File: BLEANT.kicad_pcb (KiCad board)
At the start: 4 copper layers, 75.8 x 76.2 mm, 71 parts, among them IC1 FAN4010IL6X_F113, IC2 FAN4010IL6X_F113, J1 Conn_01x04_Male, J2 SC_19-20, J3 Conn_01x02, J4 Conn_01x02, J5 1909763-1, U1 nRF51x22-QFxx, U2 LM50BIM3, U3 MP5077GG-Z, U4 MP5077GG-Z, U5 MCP2515-xSO, U6 SN65HVD1050D, X2 32.768kHz, Y1 16MHz

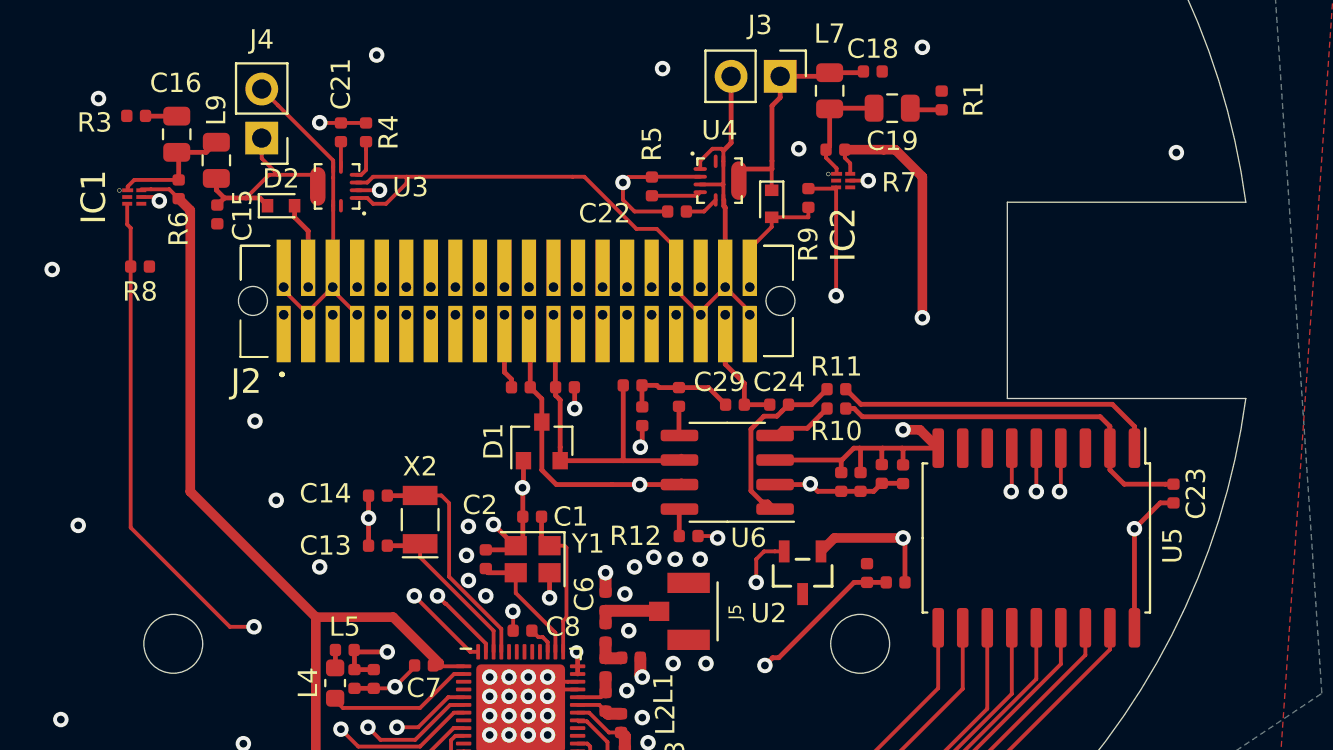
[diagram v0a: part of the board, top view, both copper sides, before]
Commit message: Added a level shifter
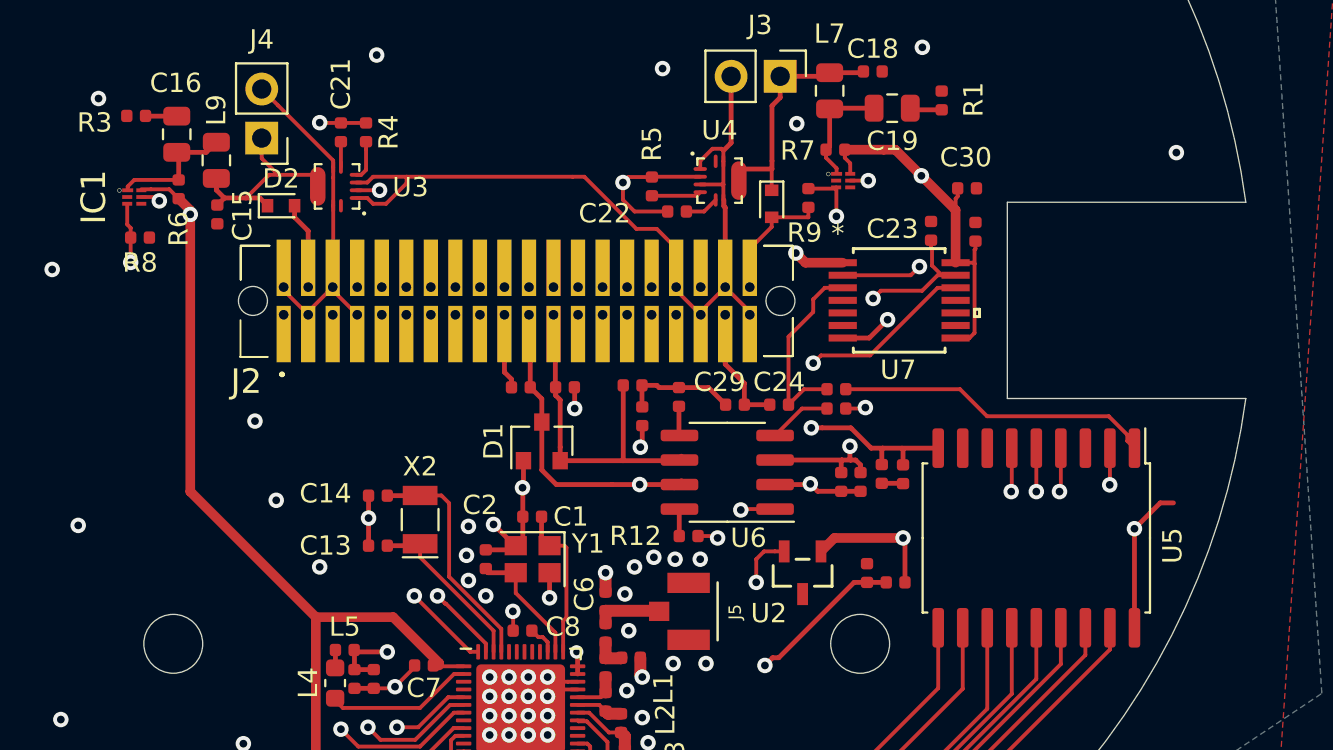
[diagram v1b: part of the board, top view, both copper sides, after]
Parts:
- added C30: 1nF, Capacitor_SMD:C_0402_1005Metric, F.Cu at (175.7, 121.2)
- added R16: 10k, Resistor_SMD:R_0402_1005Metric, F.Cu at (176.2, 123.5)
- added U7: TXB0104PWR, Level Shifter:TXB0104PWR, F.Cu at (172.2, 127.0)
- moved C23 18.5 mm to (173.8, 123.4), turned to 90 degrees
- moved R8 1.50 mm to (132.9, 123.8)
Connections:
- C17 pad 1: +5V -> +3V3
- C20 pad 2: +5V -> +3V3
- U5 pad 2: Net-(C23-Pad1) -> Net-(U5-Pad2)
- U5 pad 9: +5V -> +3V3
- U6 pad 1: Net-(C24-Pad2) -> Net-(U6-Pad1)
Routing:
- net +3V3: track 67.7 -> 122.6 mm, vias 0 -> 3
- net Net-(U5-Pad2): track 0.00 -> 22.2 mm, vias 0 -> 2
- net Net-(U6-Pad1): track 0.00 -> 21.0 mm, vias 0 -> 2
- net +5V: track 46.8 -> 54.9 mm
- net Net-(C23-Pad1): track 19.9 -> 14.4 mm, vias 0 -> 2
- net GND: track 84.1 -> 85.6 mm, vias 74 -> 75
- net 3V3Sense: track 40.7 -> 40.0 mm

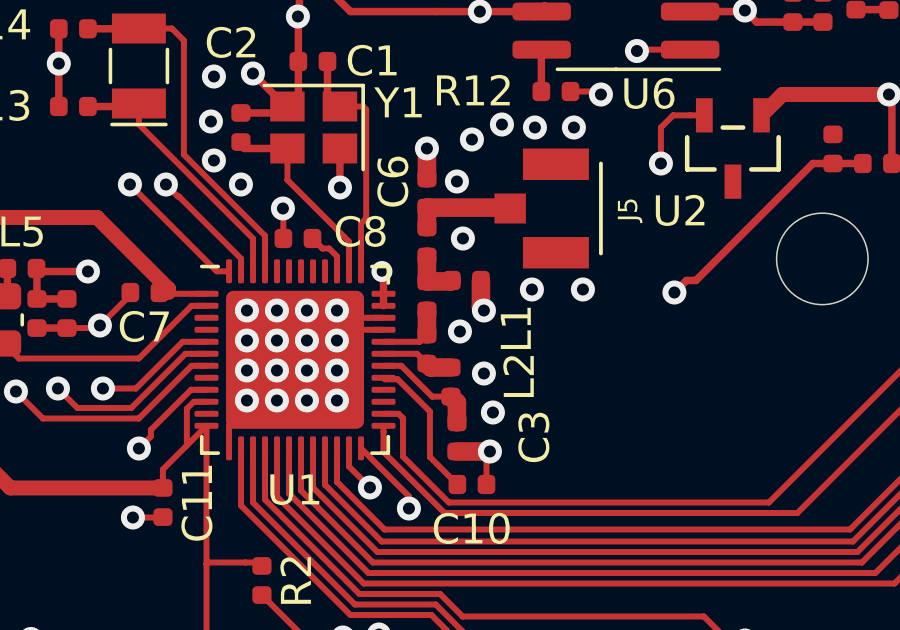
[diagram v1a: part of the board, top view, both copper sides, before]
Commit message: Changed RF traces to 50Ohm microstrips
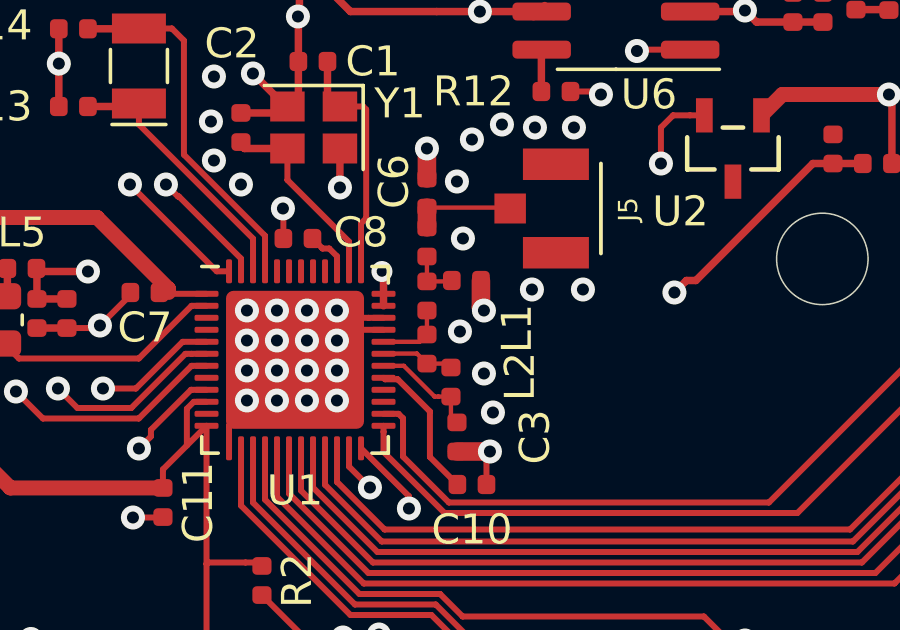
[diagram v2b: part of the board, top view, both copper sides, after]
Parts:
- U7: value TXB0104PWR -> PW14
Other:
- rule trace_min: 0.2 -> 0.1

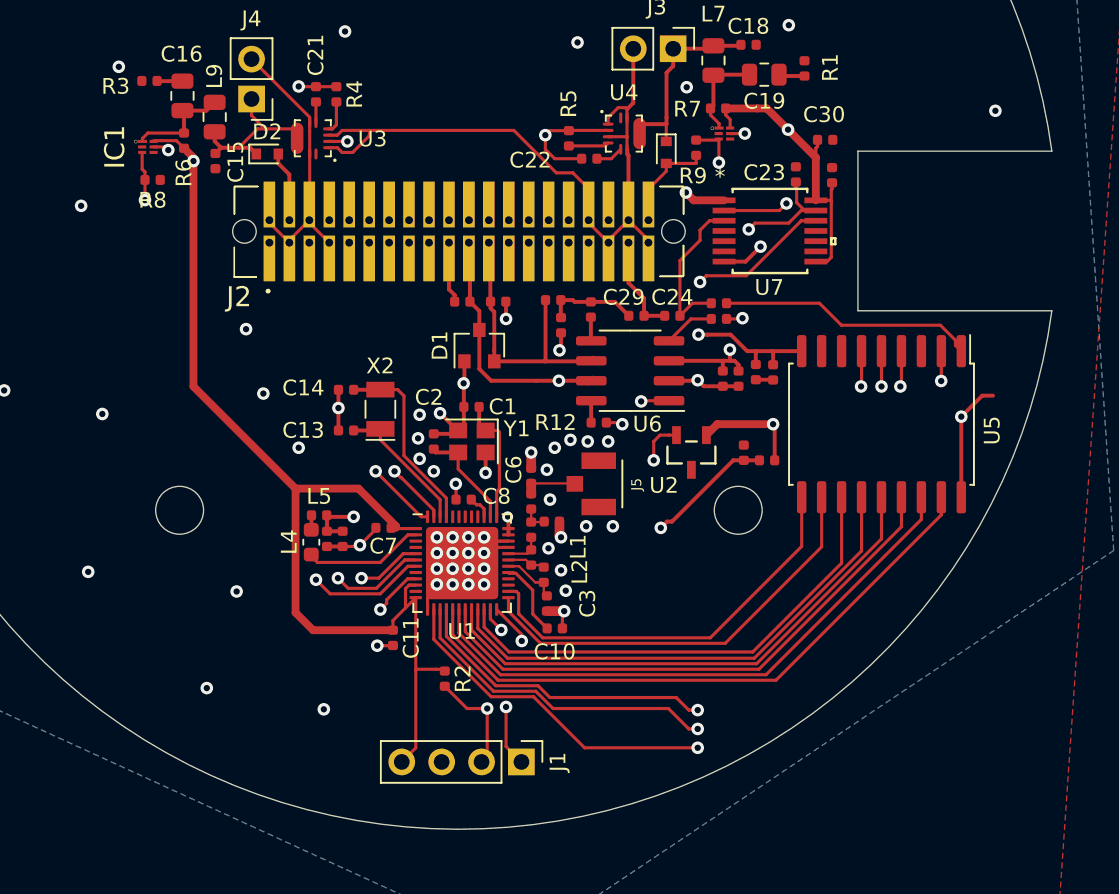
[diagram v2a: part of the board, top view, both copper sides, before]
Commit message: Added the filter and other alterations to routing. Removed copper peninsulas and improved routing overall
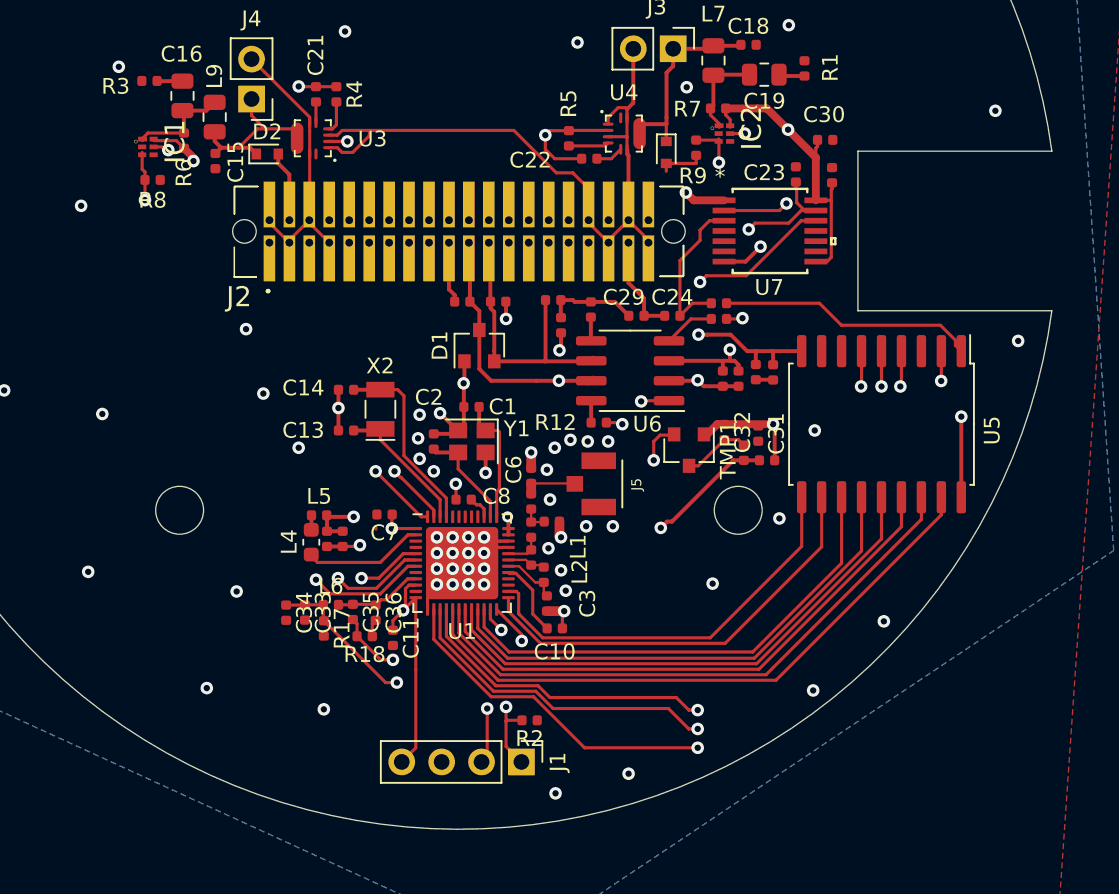
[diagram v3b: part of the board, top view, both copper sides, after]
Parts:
- removed U2: LM50BIM3, footprints:LM50_DBZ_3
- added C31: 1nF, Capacitor_SMD:C_0402_1005Metric, F.Cu at (171.4, 139.9)
- added C32: 100nF, Capacitor_SMD:C_0402_1005Metric, F.Cu at (169.3, 139.8)
- added C33: 1nF, Capacitor_SMD:C_0402_1005Metric, F.Cu at (142.6, 151.3)
- added C34: 100nF, Capacitor_SMD:C_0402_1005Metric, F.Cu at (141.4, 151.3)
- added C35: 100nF, Capacitor_SMD:C_0402_1005Metric, F.Cu at (145.7, 151.2)
- added C36: 2.2uF, Capacitor_SMD:C_0402_1005Metric, F.Cu at (147.1, 151.3)
- added L6: 2.2uH, Inductor_SMD:L_0402_1005Metric, F.Cu at (144.2, 150.8)
- added R17: 3.3k, Resistor_SMD:R_0402_1005Metric, F.Cu at (143.8, 152.3)
- added R18: 3.3, Resistor_SMD:R_0402_1005Metric, F.Cu at (146.4, 152.8)
- added TMP1: LM50CIM3X, Package_TO_SOT_SMD:SOT-23, F.Cu at (167.1, 140.9)
- IC1, IC2: footprint FAN4010:6-LEAD_MICROPAK -> MASA_Library:6-LEAD_MICROPAK
- R2: value 10k -> 1k
- U7: value PW14 -> TXB0104PWR
- moved R2 6.02 mm to (156.9, 158.2), turned to 180 degrees
- moved C7 0.85 mm to (147.7, 145.1)
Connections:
- R2 pad 1: +3V3 -> GND
- R2 pad 2: SWDIO -> SWDCLK
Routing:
- net +3V3: track 122.6 -> 32.4 mm, vias 3 -> 5
- net Net-(C33-Pad1): track 0.00 -> 47.0 mm, vias 0 -> 2
- net Temperature: track 45.6 -> 5.65 mm, vias 2 -> 0
- net SWDIO: track 14.6 -> 11.3 mm
- net GND: track 85.6 -> 87.4 mm, vias 75 -> 83
- net Net-(C36-Pad2): track 0.00 -> 1.10 mm
- net SWDCLK: track 11.2 -> 12.2 mm
- added copper zone on B.Cu, net +3V3
- removed copper zone on B.Cu, net GND

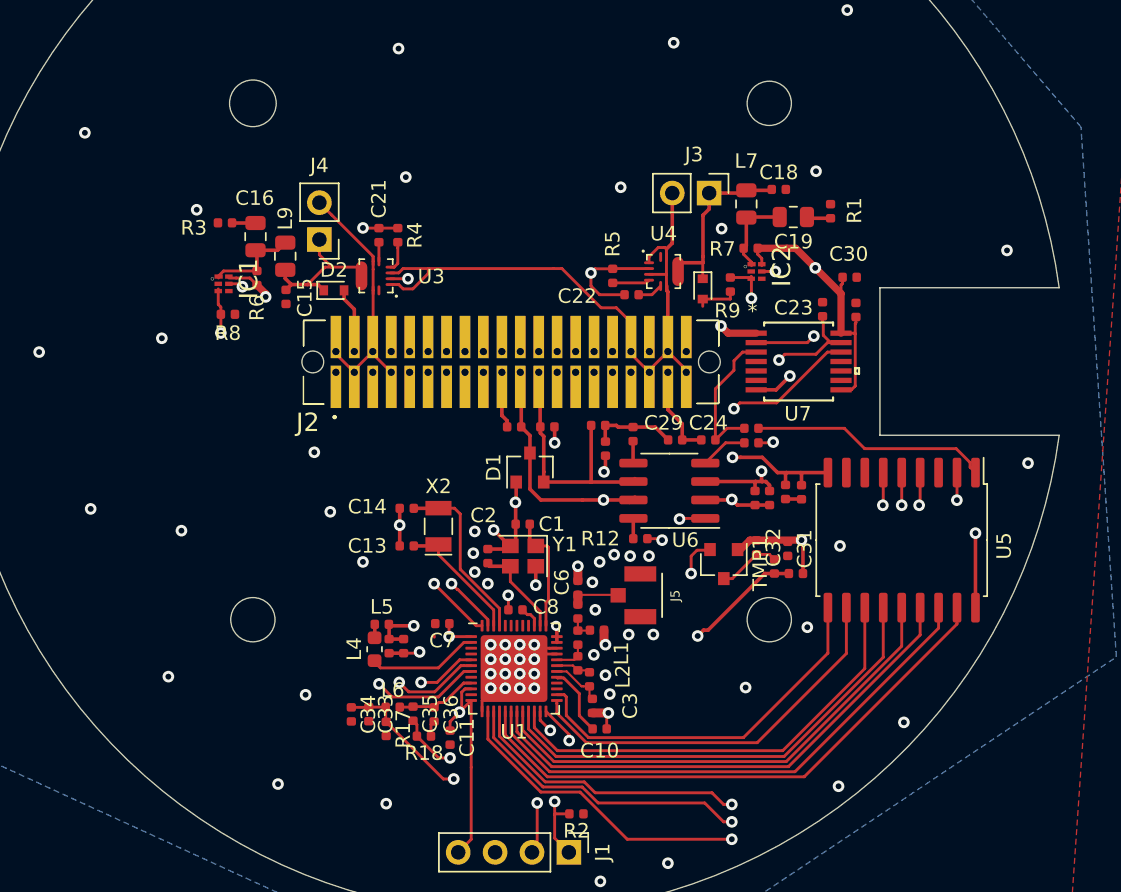
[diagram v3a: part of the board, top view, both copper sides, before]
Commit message: Added a metric ton of test points
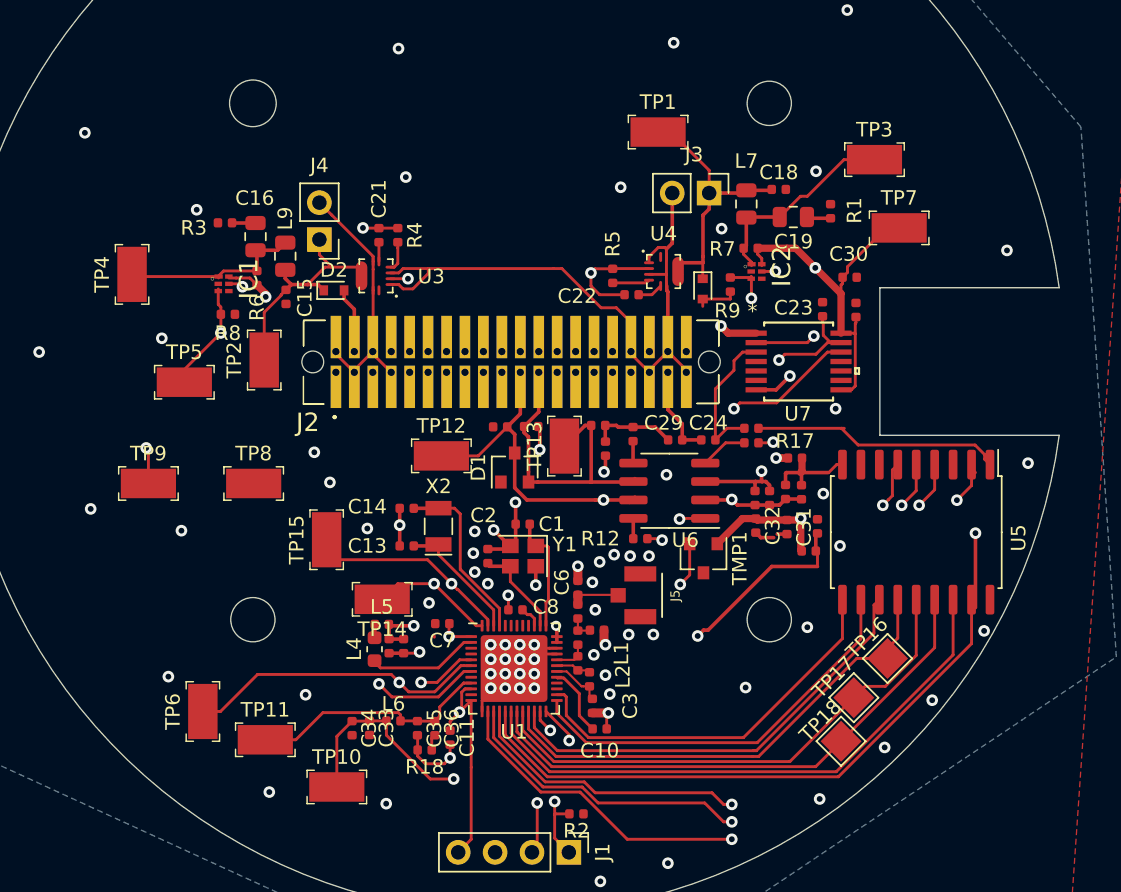
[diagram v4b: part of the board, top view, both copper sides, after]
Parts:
- added TP1: 5029, digikey-footprints:PC_Test_Point_Mini_3.8x2.03mm, F.Cu at (162.5, 111.2)
- added TP10: 5029, digikey-footprints:PC_Test_Point_Mini_3.8x2.03mm, F.Cu at (140.4, 156.3)
- added TP11: 5029, digikey-footprints:PC_Test_Point_Mini_3.8x2.03mm, F.Cu at (135.5, 153.1)
- added TP12: 5029, digikey-footprints:PC_Test_Point_Mini_3.8x2.03mm, F.Cu at (147.6, 133.5)
- added TP13: 5029, digikey-footprints:PC_Test_Point_Mini_3.8x2.03mm, F.Cu at (156.1, 132.8)
- added TP14: 5029, digikey-footprints:PC_Test_Point_Mini_3.8x2.03mm, F.Cu at (143.5, 143.4)
- added TP15: 5029, digikey-footprints:PC_Test_Point_Mini_3.8x2.03mm, F.Cu at (139.7, 139.3)
- added TP16: TestPoint, TestPoint:TestPoint_Pad_2.0x2.0mm, F.Cu at (178.3, 147.4)
- added TP17: TestPoint, TestPoint:TestPoint_Pad_2.0x2.0mm, F.Cu at (176.0, 150.2)
- added TP18: TestPoint, TestPoint:TestPoint_Pad_2.0x2.0mm, F.Cu at (175.1, 153.2)
- added TP2: 5029, digikey-footprints:PC_Test_Point_Mini_3.8x2.03mm, F.Cu at (135.4, 126.9)
- added TP3: 5029, digikey-footprints:PC_Test_Point_Mini_3.8x2.03mm, F.Cu at (177.4, 113.1)
- added TP4: 5029, digikey-footprints:PC_Test_Point_Mini_3.8x2.03mm, F.Cu at (126.3, 121.0)
- added TP5: 5029, digikey-footprints:PC_Test_Point_Mini_3.8x2.03mm, F.Cu at (129.9, 128.4)
- added TP6: 5029, digikey-footprints:PC_Test_Point_Mini_3.8x2.03mm, F.Cu at (131.2, 151.1)
- added TP7: 5029, digikey-footprints:PC_Test_Point_Mini_3.8x2.03mm, F.Cu at (179.1, 117.8)
- added TP8: 5029, digikey-footprints:PC_Test_Point_Mini_3.8x2.03mm, F.Cu at (134.7, 135.4)
- added TP9: 5029, digikey-footprints:PC_Test_Point_Mini_3.8x2.03mm, F.Cu at (127.4, 135.4)
- C21: value 0.68uF -> 47nF
- C22: value 1uF -> 47nF
- R17: value 3.3k -> 0
- moved R17 33.8 mm to (171.9, 133.7), turned to 0 degrees
- moved R14 4.05 mm to (173.5, 138.3)
- moved R15 1.78 mm to (172.9, 140.1), turned to 0 degrees
- moved C32 1.50 mm to (169.2, 138.3)
- moved C31 1.50 mm to (171.4, 138.4)
- moved TMP1 1.46 mm to (165.7, 140.6)
- moved U5 1.14 mm to (180.3, 138.8)
- moved C28 1.12 mm to (153.8, 131.5)
- moved D1 1.05 mm to (152.7, 134.3)
- moved C35 1.04 mm to (145.9, 152.2)
- moved C27 0.97 mm to (151.7, 131.5)
- moved C33 0.95 mm to (142.7, 152.2)
- moved C36 0.95 mm to (147.2, 152.2)
- moved L6 0.95 mm to (144.3, 151.8)
- moved C34 0.95 mm to (141.4, 152.2)
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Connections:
- C17 pad 1: +3V3 -> Net-(C17-Pad1)
- C20 pad 2: +3V3 -> Net-(C17-Pad1)
- R17 pad 1: Net-(C33-Pad1) -> +3V3
- R17 pad 2: GND -> Net-(C17-Pad1)
- U5 pad 9: +3V3 -> Net-(C17-Pad1)
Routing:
- net 5V0Sense: track 74.6 -> 89.4 mm
- net Temperature: track 5.65 -> 16.9 mm
- net GND: track 87.4 -> 77.2 mm, vias 83 -> 87
- net UART_RX: track 24.8 -> 34.2 mm
- net Net-(C19-Pad1): track 5.95 -> 14.1 mm
- net CAN_RST: track 39.4 -> 46.9 mm, vias 0 -> 1
- net CAN_H: track 19.4 -> 26.4 mm
- net Net-(C17-Pad1): track 0.00 -> 6.82 mm
- net Net-(C18-Pad1): track 13.4 -> 19.6 mm
- net Net-(C16-Pad1): track 6.68 -> 12.7 mm
- net +5V: track 54.9 -> 60.7 mm
- net Net-(C15-Pad1): track 11.8 -> 17.2 mm
- net +3V3: track 32.4 -> 27.1 mm, vias 5 -> 6
- net Net-(R14-Pad1): track 50.3 -> 54.9 mm
- net 3V3Sense: track 40.0 -> 44.4 mm
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
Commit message: Added some filters and stuff
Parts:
- added C37: 10nF, Capacitor_SMD:C_0402_1005Metric, F.Cu at (168.1, 125.7)
- added C38: 10nF, Capacitor_SMD:C_0402_1005Metric, F.Cu at (173.3, 124.3)
- added C39: 10nF, Capacitor_SMD:C_0402_1005Metric, F.Cu at (172.9, 122.7)
- added C40: 100pF, Capacitor_SMD:C_0402_1005Metric, F.Cu at (149.5, 144.1)
- added C41: 100pF, Capacitor_SMD:C_0402_1005Metric, F.Cu at (180.9, 145.8)
- added C42: 100pF, Capacitor_SMD:C_0402_1005Metric, F.Cu at (182.2, 145.9)
- added C43: 100pF, Capacitor_SMD:C_0402_1005Metric, F.Cu at (172.3, 152.3)
- added U2: SN74LVC1T45DBVR, digikey-footprints:SOT-23-6, F.Cu at (170.7, 127.3)
- C30: value 1nF -> 10nF
- R16: value 10k -> 470
- U7: value TXB0104PWR -> SN74LVC1T45DBVR; footprint Level Shifter:TXB0104PWR -> digikey-footprints:SOT-23-6
- moved R16 33.4 mm to (148.9, 142.8), turned to 315 degrees
- moved C23 7.61 mm to (169.4, 129.6), turned to 180 degrees
- moved U7 3.23 mm to (175.3, 127.7)
- moved C30 2.30 mm to (175.9, 123.5)
- moved TP6 1.50 mm to (130.4, 152.4)
- moved TP9 1.36 mm to (126.1, 135.2)
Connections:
- C30 pad 2: +5V -> +3V3
- R16 pad 1: +5V -> UART_RX
- R16 pad 2: GND -> Net-(C40-Pad1)
- U1 pad 47: UART_RX -> Net-(C40-Pad1)
- U5 pad 2: Net-(U5-Pad2) -> Net-(U2-Pad3)
- U7 pad 2: Net-(U5-Pad2) -> GND
- U7 pad 4: Net-(U7-Pad4) -> Net-(U6-Pad1)
- U7 pad 5: Net-(U7-Pad5) -> +3V3
- U7 pad 6: Net-(U7-Pad6) -> +5V
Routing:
- net Net-(U2-Pad3): track 0.00 -> 27.9 mm, vias 0 -> 2
- net Net-(U5-Pad2): track 26.0 -> 0.00 mm, vias 2 -> 0
- net GND: track 77.2 -> 94.5 mm, vias 87 -> 89
- net Net-(C23-Pad1): track 14.4 -> 7.04 mm
- net +5V: track 60.7 -> 53.9 mm
- net +3V3: track 27.1 -> 31.6 mm, vias 6 -> 8
- net UART_RX: track 34.2 -> 30.2 mm
- net Net-(C40-Pad1): track 0.00 -> 2.73 mm
- net Net-(U6-Pad1): track 21.0 -> 22.3 mm
- net Net-(C24-Pad2): track 10.2 -> 11.5 mm
- net MOSI: track 36.2 -> 37.0 mm
- net MISO: track 37.9 -> 38.5 mm
- net SCK: track 33.2 -> 33.9 mm
- net (no net): vias 1 -> 0
